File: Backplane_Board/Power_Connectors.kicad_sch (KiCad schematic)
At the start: 27 parts, among them J10 Conn_01x02_Pin, J11 Conn_01x02_Pin, J12 Conn_01x02_Pin, J13 Conn_01x02_Pin, J14 Conn_01x02_Pin, J15 Conn_01x02_Pin, J16 Conn_01x02_Pin, J17 Conn_01x02_Pin, J18 Conn_01x02_Pin, J19 Conn_01x02_Pin, J20 Conn_01x02_Pin, J21 Conn_01x02_Pin, J22 Conn_01x02_Pin, J23 Conn_01x02_Pin, J24 Conn_01x02_Pin, J6 Conn_01x02_Pin, J7 Conn_01x02_Pin, J8 Conn_01x02_Pin, J9 Conn_01x02_Pin, U5 PKU3511SPI

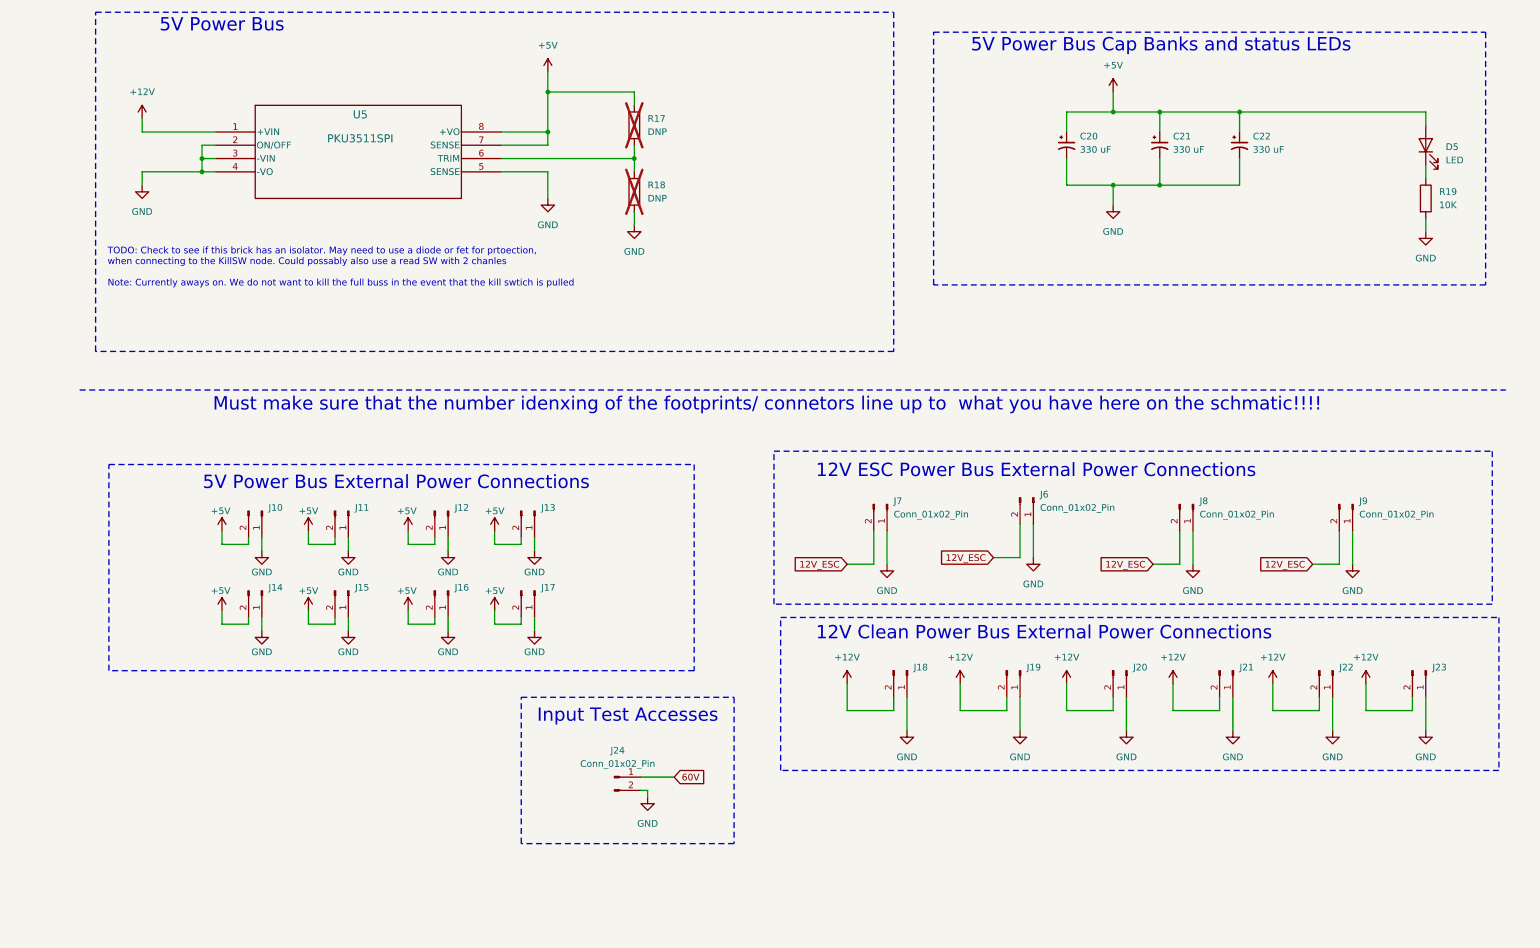
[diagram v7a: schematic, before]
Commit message: adding more footprints
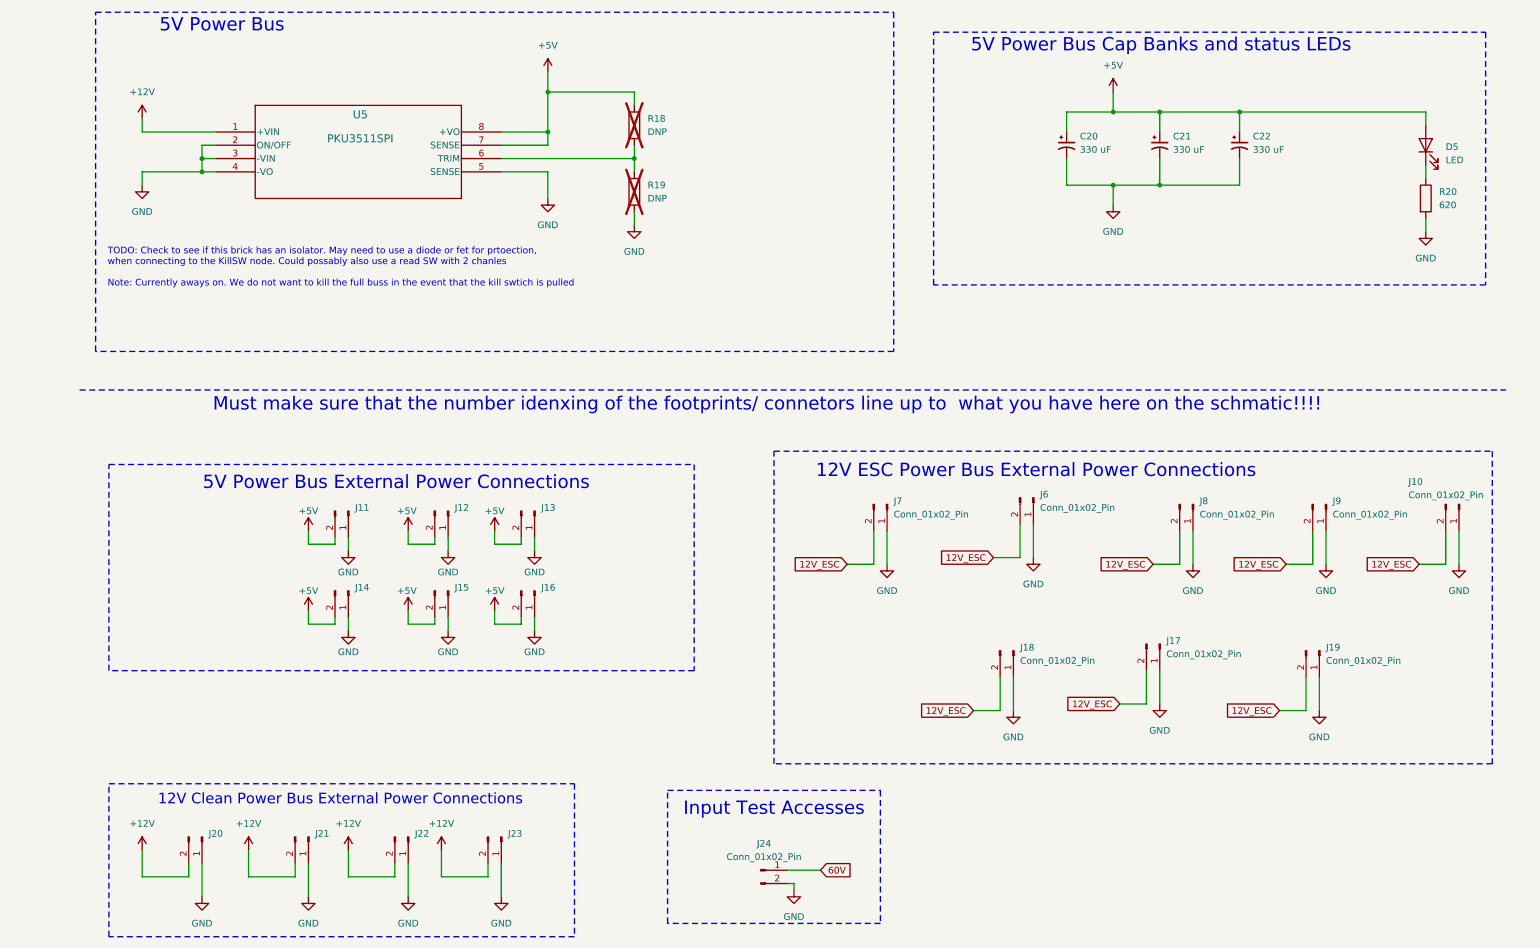
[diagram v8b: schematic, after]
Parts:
- D5: footprint (none) -> LED_SMD:LED_0603_1608Metric
- J10, J17, J18, J19, J6, J7, J8, J9: footprint (none) -> Connector_AMASS:AMASS_XT30U-M_1x02_P5.0mm_Vertical
- J11, J12, J13, J14, J15, J16: footprint (none) -> TerminalBlock:TerminalBlock_Xinya_XY308-2.54-2P_1x02_P2.54mm_Horizontal
- J20, J21, J22, J23: footprint (none) -> TerminalBlock_4Ucon:TerminalBlock_4Ucon_1x02_P3.50mm_Horizontal
- J24: footprint (none) -> TestPoint:TestPoint_2Pads_Pitch2.54mm_Drill0.8mm
- R18: renamed from R17; footprint (none) -> Inductor_SMD:L_1206_3216Metric
- R19: renamed from R18; footprint (none) -> Inductor_SMD:L_1206_3216Metric
- R20: renamed from R19; value 10K -> 620; footprint (none) -> Resistor_SMD:R_1206_3216Metric_Pad1.30x1.75mm_HandSolder
- U5: footprint PKU 3500S_FPM -> PKU3511SPI:PKU 3500S_FPM
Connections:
- net +12V: no longer J18.2 (Pin_2), J19.2 (Pin_2)
- net +5V: no longer J10.2 (Pin_2), J17.2 (Pin_2)
- net 12V_ESC: now also J10.2 (Pin_2), J17.2 (Pin_2), J18.2 (Pin_2), J19.2 (Pin_2)
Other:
- moved on the sheet: J20, J21, J22, J23, J24, J9
